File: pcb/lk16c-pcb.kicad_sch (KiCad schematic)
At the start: 46 parts, among them J1 Conn_01x03, J2 Conn_01x04, J3 Conn_01x04, J5 Conn_01x04, J6 Conn_01x04, J7 Conn_01x04, J8 Conn_01x04, J9 Conn_01x04, SW1 SW_Push, SW10 SW_Push, SW11 SW_Push, SW12 SW_Push, SW13 SW_Push, SW14 SW_Push, SW15 SW_Push, SW16 SW_Push, SW17 SW_Push, SW2 SW_Push, SW3 SW_Push, SW4 SW_Push, SW5 SW_Push, SW6 SW_Push, SW7 SW_Push, SW8 SW_Push, SW9 SW_Push, U1 RaspberryPi_Pico

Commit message: Update board to board connector
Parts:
- J1: renamed from J3; footprint LKBD_Connector:PinHeader_1x04_THT_P2.54mm_nSilk -> Connector:EdgeHeader_1x04_THT_P2.54mm_Right
- J2: footprint LKBD_Connector:PinHeader_1x04_THT_P2.54mm_nSilk -> Connector:EdgeHeader_1x04_THT_P2.54mm_Left
- J3: renamed from J5; footprint LKBD_Connector:PinHeader_1x04_THT_P2.54mm_nSilk -> Connector:EdgeHeader_1x04_THT_P2.54mm_Right
- J4: renamed from J7; footprint LKBD_Connector:PinHeader_1x04_THT_P2.54mm_nSilk -> Connector:EdgeHeader_1x04_THT_P2.54mm_Left
- J5: renamed from J6; footprint LKBD_Connector:PinHeader_1x04_THT_P2.54mm_nSilk -> Connector:EdgeHeader_1x04_THT_P2.54mm_Right
- J6: renamed from J8; footprint LKBD_Connector:PinHeader_1x04_THT_P2.54mm_nSilk -> Connector:EdgeHeader_1x04_THT_P2.54mm_Left
- renumbered J1 to J7, J9 to J8
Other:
- moved on the sheet: H1, H2, H3, H4, J1, J2, J4, J5, J7, J8

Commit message: Update LKBD and move edge connectors to leave space for an LED stirp
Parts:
- removed J7: Conn_01x03, LKBD_Connector:PinHeader_1x03_THT_P2.54mm_nSilk, symbol Connector_Generic:Conn_01x03
- removed J8: Conn_01x04, LKBD_Connector:PinHeader_1x04_THT_P2.54mm_nSilk, symbol Connector_Generic:Conn_01x04
- added J7: PINHD_1x03_ARGB, LKBD_Connector:PinHeader_1x03_THT_P2.54mm_nSilk, symbol LKBD_Connector:PINHD_1x03_ARGB
- added J8: PINHD_1x05_I2C, LKBD_Connector:PinHeader_1x05_THT_P2.54mm_nSilk, symbol LKBD_Connector:PINHD_1x05_I2C
- D1, D10, D11, D12, D13, D14, D16, D17, D2, D3, D4, D5, D6, D7, D8, D9: JLC SOD-323 -> SOD-123
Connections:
- net +3.3V: now also J8.2 (VCC)
- net +5V: now also J7.1 (5V)
- net GND: now also J7.3 (GND), J8.1 (GND)
- net LED_IO: now also J7.2 (DIN)
- net SCL: now also J8.4 (SCL)
- net SDA: now also J8.3 (SDA)
- net IO1: now reaches U1.2 (GPIO1)
- net IO1: now also J8.5 (IO1)
- no-connect marks 12 -> 11

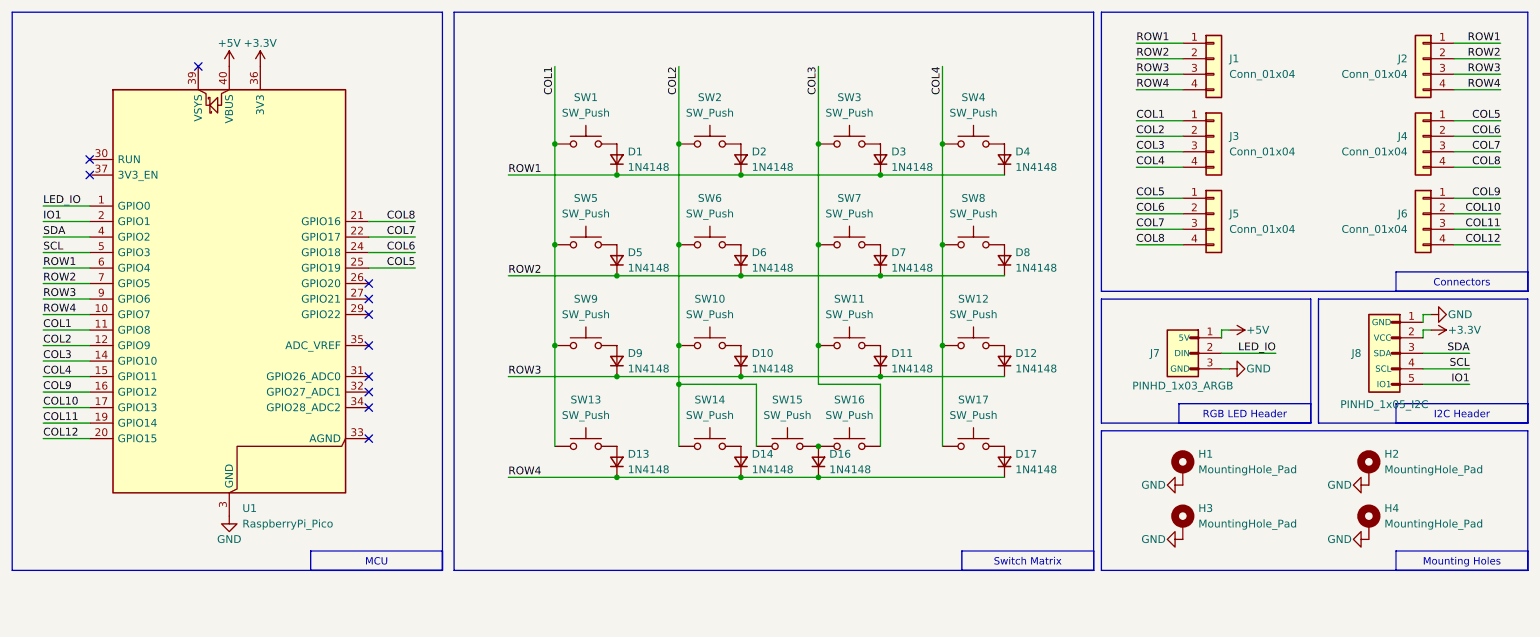
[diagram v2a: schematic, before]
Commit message: Add ability to use 2× 2U Spacebars as the bottom row (#3)
* Add ability to use 2× 2U Spacebars as the bottom row
* Move Fab DataMatrix footprint
* Add plate variant for 2space
* Fix mounting hole paste
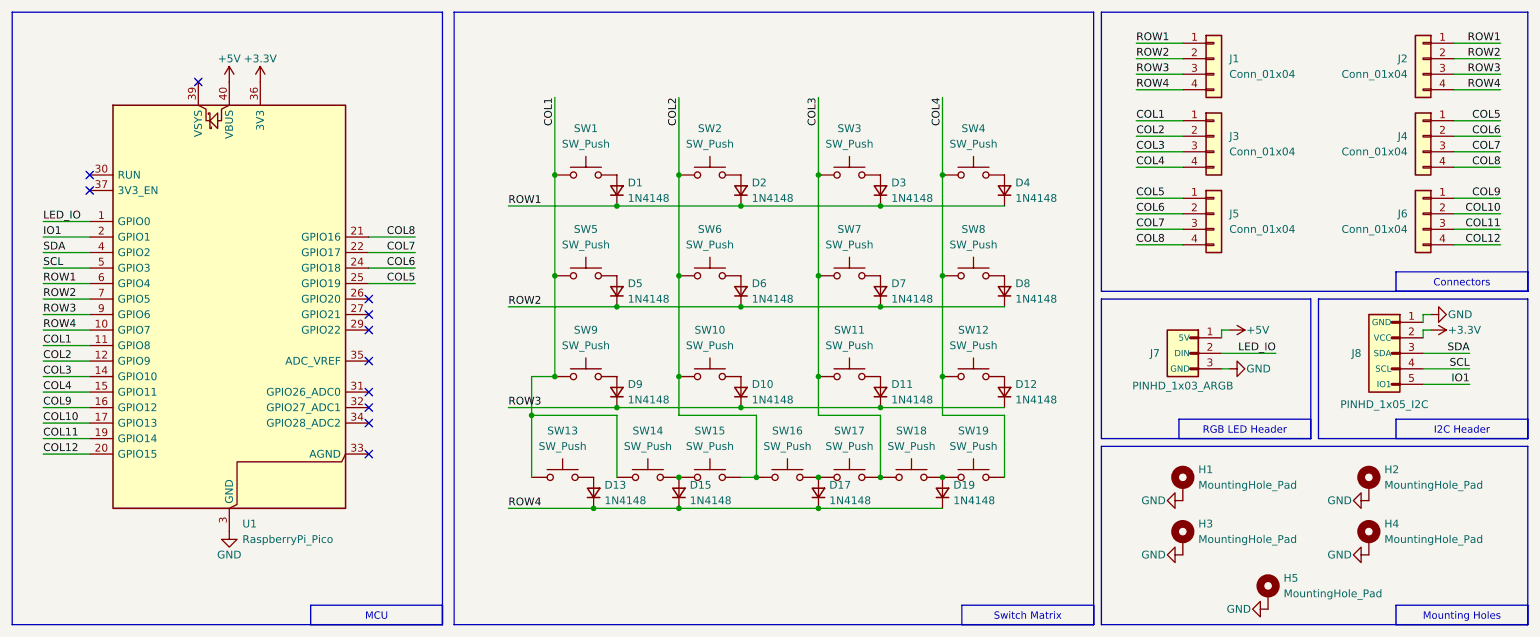
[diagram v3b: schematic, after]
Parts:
- added H5: MountingHole_Pad, LKBD_MountingHole:MountingHole_M2, symbol Mechanical:MountingHole_Pad
- added SW14, SW18: SW_Push, LKBD_KeySwitch:SW_MX_Slim_HotSwap_THT_sqSilk, symbol Switch:SW_Push
- renumbered D14 to D15, D16 to D17, D17 to D19, SW14 to SW15, SW15 to SW16, SW16 to SW17, SW17 to SW19
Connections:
- net COL1: now also SW14.2
- net COL3: now also SW18.2
- net GND: now also H5.1
- net at D15.2 (A), SW15.1: now also SW14.1
- net at D19.2 (A), SW19.1: now also SW18.1
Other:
- moved on the sheet: D1, D10, D11, D12, D13, D15, D17, D19, D2, D3, D4, D5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
